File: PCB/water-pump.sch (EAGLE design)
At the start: 27 parts, among them U1 LDL1117S12R, U3 ATSAMD11C14A-SSUT

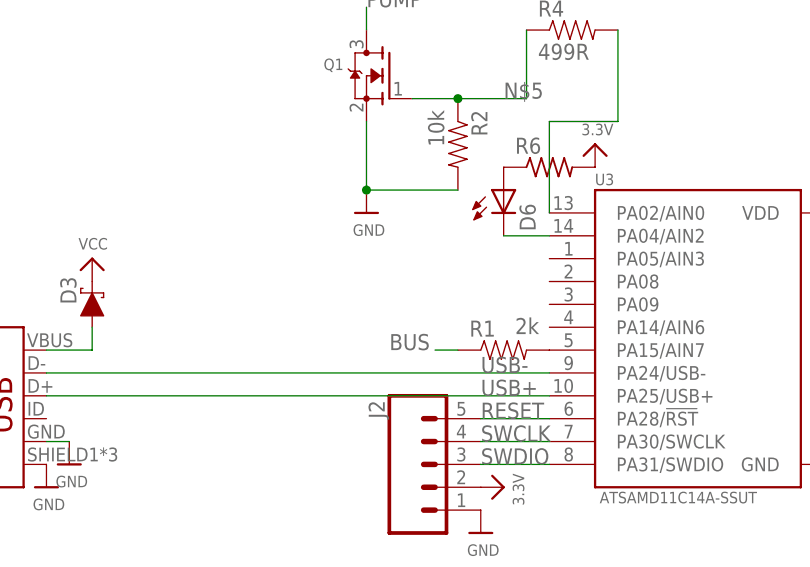
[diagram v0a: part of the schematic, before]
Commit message: added 4pin connector for remaining pins on all boards
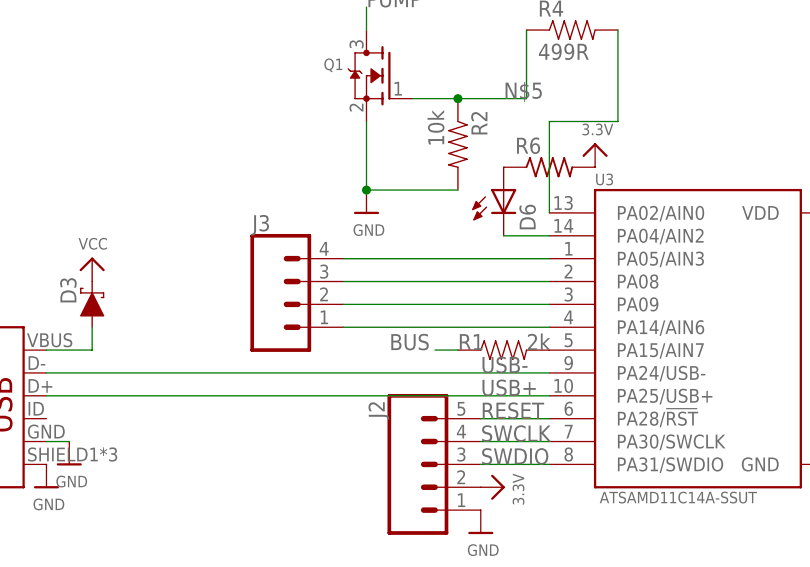
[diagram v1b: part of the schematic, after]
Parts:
- added J3: (no value), SparkFun-Connectors:CONN_04PTH
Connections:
- new net N$10: J3.2, U3.PA09
- new net N$11: J3.1, U3.PA14/AIN6
- new net N$4: J3.4, U3.PA05/AIN3
- new net N$9: J3.3, U3.PA08
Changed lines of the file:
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@@
 <?xml version="1.0" encoding="utf-8"?>
 <!DOCTYPE eagle SYSTEM "eagle.dtd">
-<eagle version="9.3.0">
+<eagle version="9.2.2">
 <drawing>
 <settings>
@@
 <part name="P+7" library="supply1" library_urn="urn:adsk.eagle:library:371" deviceset="VCC" device=""/>
 <part name="R4" library="SparkFun-Resistors" deviceset="RESISTOR" device="1206" value="499R"/>
+<part name="J3" library="SparkFun-Connectors" deviceset="CONN_04" device="PTH"/>
 </parts>
 <sheets>
@@
 </instance>
 <instance part="R1" gate="G$1" x="-48.26" y="45.72" smashed="yes">
-<attribute name="NAME" x="-52.07" y="47.2186" size="1.778" layer="95"/>
-<attribute name="VALUE" x="-46.99" y="47.498" size="1.778" layer="96"/>
+<attribute name="NAME" x="-53.34" y="45.72" size="1.778" layer="95"/>
+<attribute name="VALUE" x="-45.72" y="45.72" size="1.778" layer="96"/>
 </instance>
 <instance part="FRAME1" gate="G$1" x="-114.3" y="-81.28" smashed="yes">
@@
 <attribute name="NAME" x="-44.45" y="82.7786" size="1.778" layer="95"/>
 <attribute name="VALUE" x="-44.45" y="77.978" size="1.778" layer="96"/>
+</instance>
+<instance part="J3" gate="J1" x="-71.12" y="50.8" smashed="yes">
+<attribute name="VALUE" x="-76.2" y="43.434" size="1.778" layer="96" font="vector"/>
+<attribute name="NAME" x="-76.2" y="58.928" size="1.778" layer="95" font="vector"/>
 </instance>
 </instances>
@@
 </segment>
 </net>
+<net name="N$4" class="0">
+<segment>
+<pinref part="U3" gate="G$1" pin="PA05/AIN3"/>
+<wire x1="-43.18" y1="55.88" x2="-66.04" y2="55.88" width="0.1524" layer="91"/>
+<pinref part="J3" gate="J1" pin="4"/>
+</segment>
+</net>
+<net name="N$9" class="0">
+<segment>
+<pinref part="U3" gate="G$1" pin="PA08"/>
+<wire x1="-43.18" y1="53.34" x2="-66.04" y2="53.34" width="0.1524" layer="91"/>
+<pinref part="J3" gate="J1" pin="3"/>
+</segment>
+</net>
+<net name="N$10" class="0">
+<segment>
+<pinref part="U3" gate="G$1" pin="PA09"/>
+<wire x1="-43.18" y1="50.8" x2="-66.04" y2="50.8" width="0.1524" layer="91"/>
+<pinref part="J3" gate="J1" pin="2"/>
+</segment>
+</net>
+<net name="N$11" class="0">
+<segment>
+<pinref part="U3" gate="G$1" pin="PA14/AIN6"/>
+<wire x1="-43.18" y1="48.26" x2="-66.04" y2="48.26" width="0.1524" layer="91"/>
+<pinref part="J3" gate="J1" pin="1"/>
+</segment>
+</net>
